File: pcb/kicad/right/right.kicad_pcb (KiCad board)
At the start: 2 copper layers, 135.9 x 89.5 mm, 61 parts, among them J1 USB_C_Receptacle_USB2.0, J2 AudioJack4, J3 Conn_01x12_Male, SW1 BOOT, SW10 SW_Push, SW12 SW_Push, SW13 SW_Push, SW14 SW_Push, SW15 SW_Push, SW17 SW_Push, SW18 SW_Push, SW19 SW_Push, SW2 RESET, SW21 SW_Push, SW22 SW_Push, SW23 SW_Push, SW24 SW_Push, SW3 SW_Push, SW31 SW_Push, SW32 SW_Push, SW33 SW_Push, SW34 SW_Push, SW4 SW_Push, SW5 SW_Push, SW7 SW_Push, SW8 SW_Push, SW9 SW_Push, U1 STM32, U2 LDO

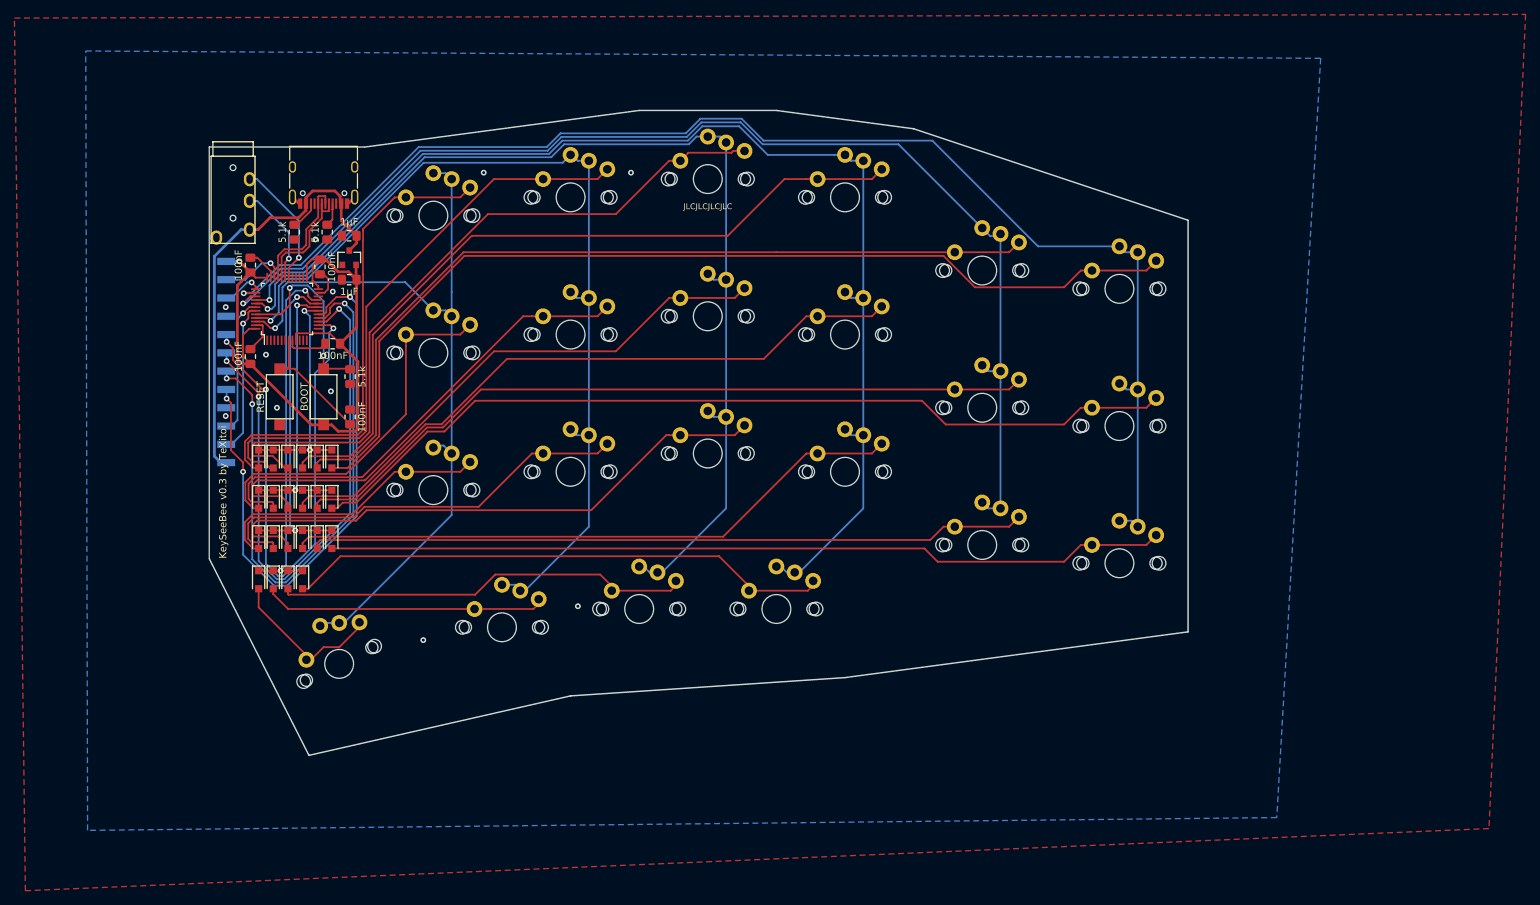
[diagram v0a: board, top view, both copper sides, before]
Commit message: Re-design the layout
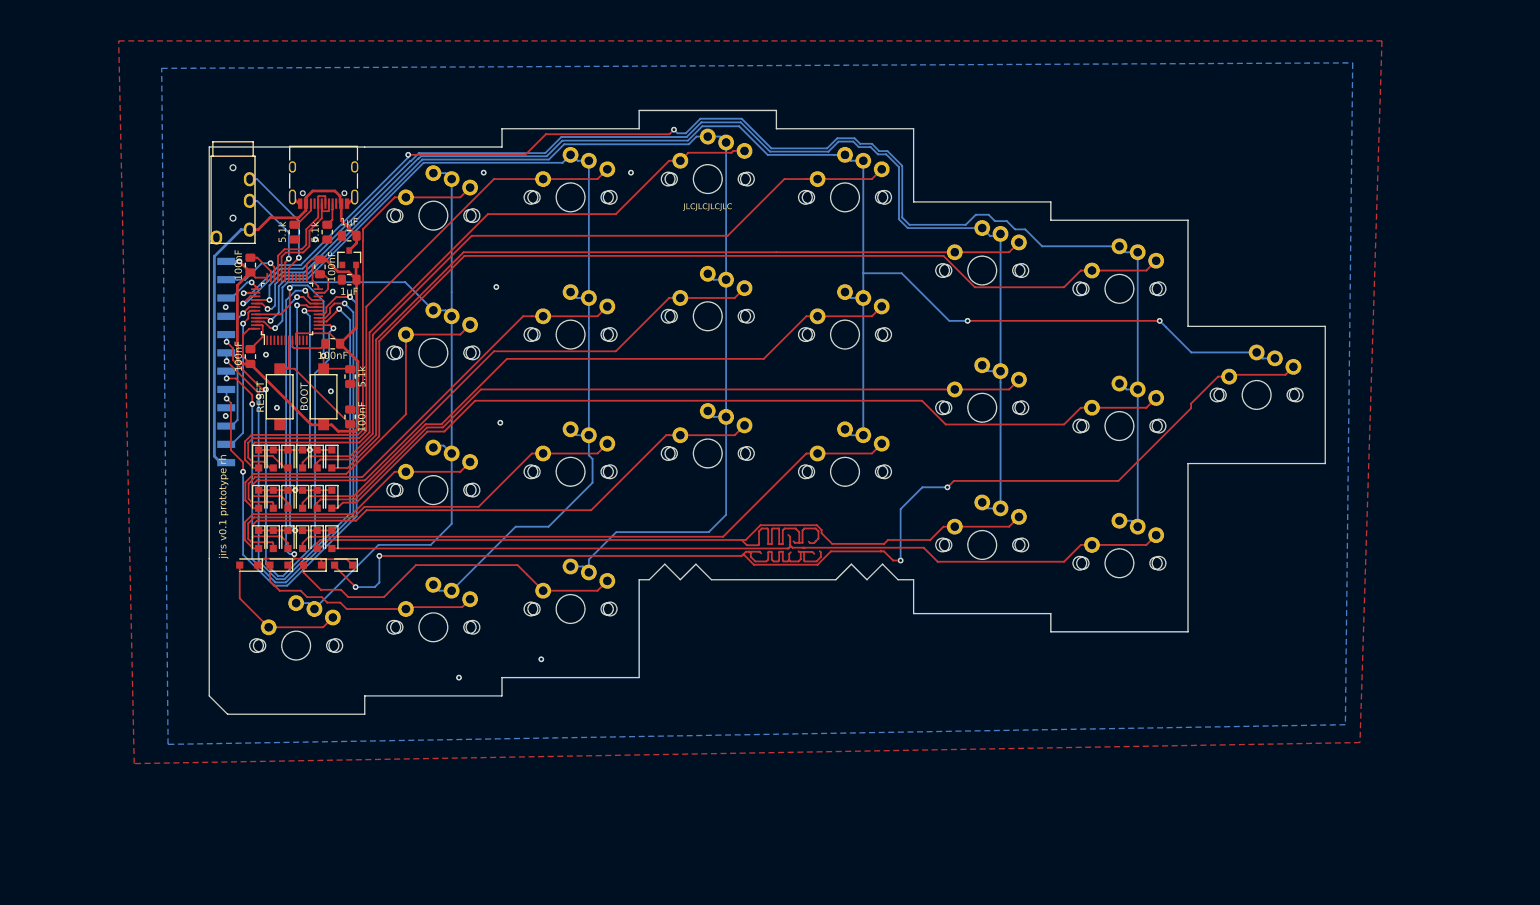
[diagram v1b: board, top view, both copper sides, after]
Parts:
- moved SW10 73.0 mm to (226.3, 99.3)
- moved SW24 9.53 mm to (131.1, 129.0)
- moved SW34 9.53 mm to (112.0, 131.6)
- moved SW15 6.49 mm to (93.0, 134.1), turned to 0 degrees
- moved D12 6.05 mm to (99.5, 122.9), turned to 180 degrees
- moved D26 3.97 mm to (95.2, 122.9), turned to 180 degrees
- moved D17 2.45 mm to (86.4, 122.9), turned to 180 degrees
- moved D36 2.18 mm to (90.6, 122.9), turned to 180 degrees
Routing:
- net Net-(D12-Pad2): track 75.9 -> 181.2 mm, vias 0 -> 4
- net COL3: track 167.2 -> 203.4 mm, vias 1 -> 3
- net Net-(D21-Pad2): track 99.7 -> 130.7 mm
- net COL4: track 149.6 -> 161.3 mm
- net Net-(D26-Pad2): track 57.9 -> 48.5 mm
- net ROW4: track 49.6 -> 58.5 mm
- net Net-(D36-Pad2): track 39.7 -> 32.2 mm
- net COL5: track 131.1 -> 138.4 mm
- net COL1: track 187.5 -> 194.7 mm, vias 1 -> 3
- net COL2: track 168.2 -> 173.6 mm
- net COL6: track 111.5 -> 115.6 mm
- net Net-(D17-Pad2): track 22.4 -> 19.8 mm
- net Net-(D7-Pad2): track 116.7 -> 119.0 mm
- net GND: vias 11 -> 13
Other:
- board size 135.9 x 89.5 mm -> 154.9 x 83.8 mm
- board text added: "jirs v0.1 prototype rh"
- board text removed: "KeySeeBee v0.3 by TeXitoi"
